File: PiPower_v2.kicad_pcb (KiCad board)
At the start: 2 copper layers, 56 x 60 mm, 80 parts, among them J1 MicroUSB_in, J10 5V_Pi, J11 12V_Out, J12 5V_IN, J2 LiPo_JST, J3 USB_A_out, J4 Auto_On, J5 5V_USB, J6 5V_EXT, J7 5V_OUT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

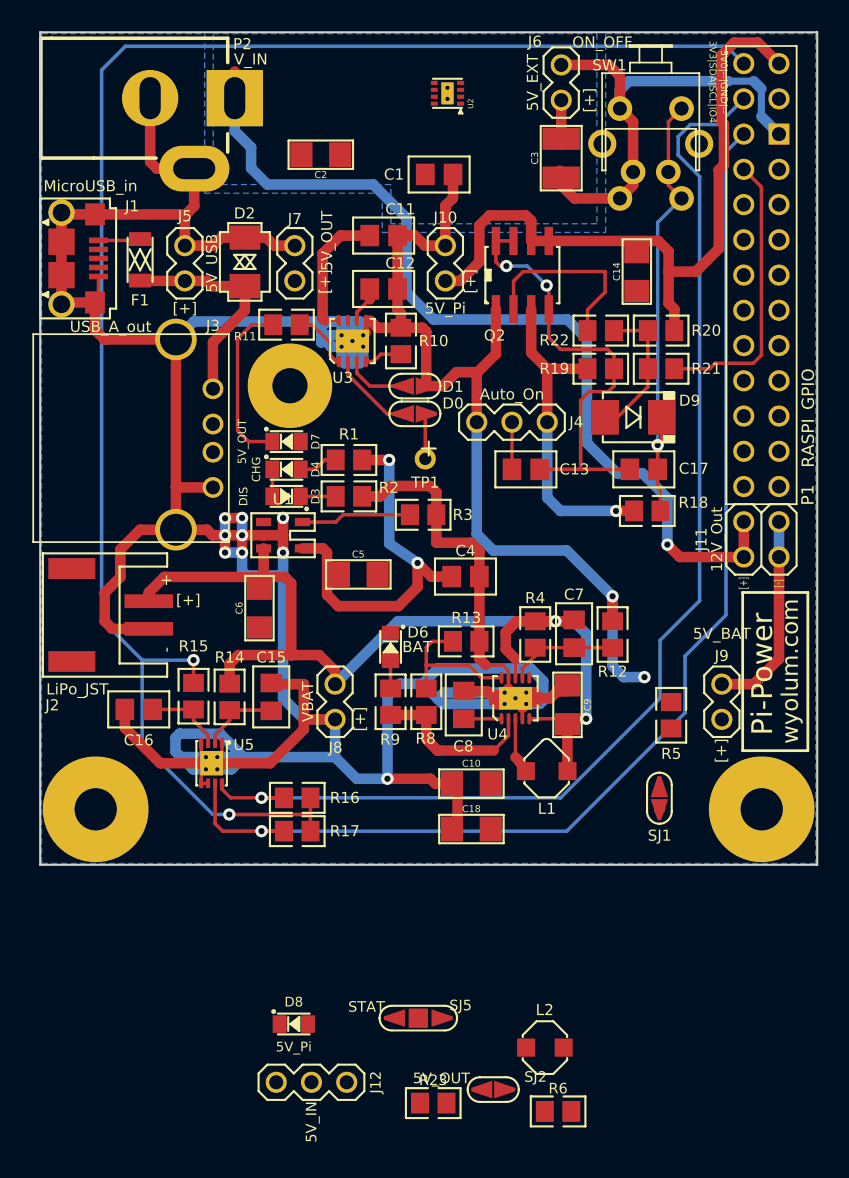
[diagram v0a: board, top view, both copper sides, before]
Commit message: 1311050158 preliminary track layout complete
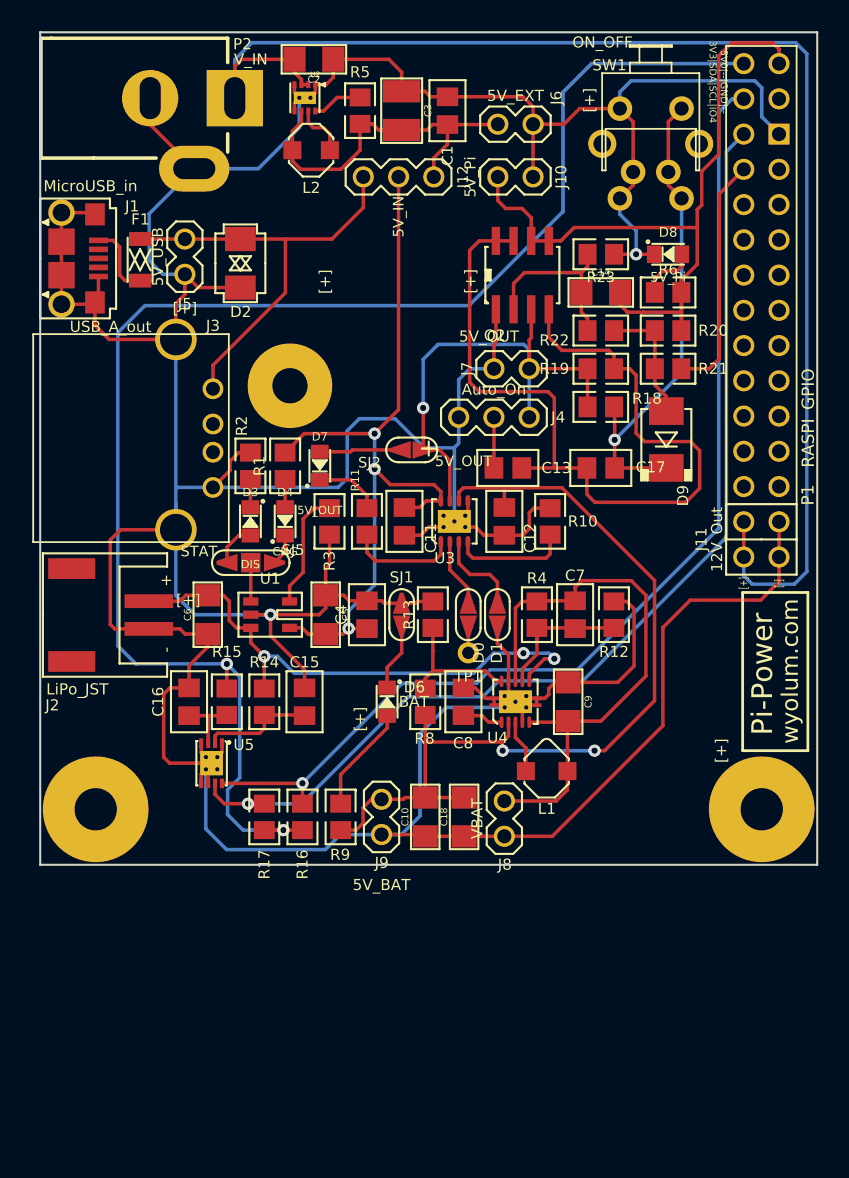
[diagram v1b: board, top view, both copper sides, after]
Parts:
- moved L2 66.8 mm to (111.3, 27.2), turned to 180 degrees
- moved J12 65.6 mm to (117.6, 29.2)
- moved R23 62.4 mm to (132.2, 34.8), turned to 180 degrees
- moved D8 61.7 mm to (137.0, 34.8)
- moved R6 59.6 mm to (137.0, 37.5)
- moved R5 49.0 mm to (114.8, 24.4), turned to 90 degrees
- moved SJ2 46.5 mm to (118.5, 48.9), turned to 180 degrees
- moved SJ5 35.0 mm to (106.9, 57.0)
- moved J9 25.9 mm to (116.3, 75.3), turned to 270 degrees
- moved SJ1 22.8 mm to (117.8, 60.7), turned to 90 degrees
- moved C11 20.7 mm to (118.0, 54.0), turned to 270 degrees
- moved C12 18.9 mm to (125.2, 54.0), turned to 270 degrees
- moved SJ4 17.5 mm to (124.7, 60.7), turned to 270 degrees
- moved J7 17.4 mm to (125.7, 43.0), turned to 180 degrees
- moved R10 16.9 mm to (128.5, 54.0)
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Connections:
- SJ5 pad 2: N-0000014 -> /STAT
- SJ5 pad 3: /STAT -> N-0000014
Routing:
- net /5V_BAT: track 14.9 -> 64.5 mm, vias 0 -> 2
- net /PWR_IN: track 66.6 -> 100.6 mm, vias 1 -> 0
- net N-0000021: track 32.7 -> 62.0 mm, vias 2 -> 0
- net /5V_EXT: track 3.18 -> 25.9 mm
- net GND: track 410.0 -> 389.3 mm, vias 11 -> 2
- net /5V_IN: track 37.3 -> 55.9 mm, vias 2 -> 3
- net /5V_USB: track 16.1 -> 32.2 mm
- net /5V_OUT: track 23.6 -> 36.1 mm
- net /SDA_Pi: track 86.6 -> 77.1 mm
- net /3V3_Pi: track 119.3 -> 109.8 mm
- net /SCL_Pi: track 87.2 -> 77.8 mm
- net N-0000035: track 12.4 -> 4.77 mm
- net /VBAT: track 74.1 -> 81.6 mm, vias 2 -> 3
- net N-0000011: track 0.00 -> 5.86 mm
- net N-000007: track 1.98 -> 7.72 mm
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- removed copper zone on B.Cu, net /5V_EXT
- removed copper zone on B.Cu, net GND

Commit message: 1311051633 track layout complete
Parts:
- moved J12 1.30 mm to (117.6, 30.5)
- moved SW1 1.00 mm to (134.8, 24.2)
- moved TP1 0.20 mm to (122.6, 63.3)
- moved J8 0.12 mm to (125.2, 75.3)
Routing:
- net GND: track 389.3 -> 404.4 mm
- net /5V_BAT: track 64.5 -> 70.4 mm
- net /3V3_Pi: track 109.8 -> 113.6 mm
- net /VBAT: track 81.6 -> 84.3 mm
- net /GPIO4: track 17.4 -> 20.1 mm
- net /5V_EXT: track 25.9 -> 28.1 mm
- net /SCL_Pi: track 77.8 -> 79.9 mm
- net /5V_Pi: track 51.0 -> 52.5 mm
- net /5V_USB: track 32.2 -> 30.9 mm
- net /5V_IN: track 55.9 -> 54.6 mm
- net /SDA_Pi: track 77.1 -> 77.8 mm
- net N-0000021: track 62.0 -> 61.5 mm
- added copper zone on B.Cu, net GND
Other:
- net class 15mil added: clearance 0.0635, trace_width 0.381, via_dia 0.889, via_drill 0.635
- board text added: "ON<>OFF"
- board text added: "rev 2"

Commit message: 1311051958 added some zones
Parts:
- moved J12 8.15 mm to (117.6, 38.6)
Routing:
- net /3V3_Pi: track 113.6 -> 101.9 mm
- net /5V_EXT: track 28.1 -> 36.3 mm
- net /5V_IN: track 54.6 -> 46.5 mm
- net /5V_USB: track 30.9 -> 28.2 mm
- net N-0000021: track 61.5 -> 60.8 mm
- net N-0000022: track 12.9 -> 12.4 mm
- added copper zone on F.Cu, net /5V_EXT
- added copper zone on F.Cu, net /5V_Pi

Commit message: 1311051125 added more zones
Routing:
- net GND: track 404.4 -> 391.6 mm
- net N-000007: track 7.72 -> 9.18 mm
- added copper zone on F.Cu, net /5V_BAT
- added copper zone on F.Cu, net /5V_USB
- added copper zone on F.Cu, net /VBAT
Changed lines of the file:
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@@
     (thickness 1.6)
     (drawings 31)
-    (tracks 606)
+    (tracks 596)
     (zones 0)
     (modules 80)
@@
   (segment (start 102.247 59.328) (end 103.825 59.328) (width 0.762) (layer F.Cu) (net 21) (status 20))
   (segment (start 101.82322 59.75178) (end 102.247 59.328) (width 0.762) (layer F.Cu) (net 21))
+  (segment (start 144.995 56.57) (end 144.995 66.955) (width 0.762) (layer F.Cu) (net 22) (status 400000))
+  (segment (start 135.38 76.57) (end 125.2 76.57) (width 0.762) (layer F.Cu) (net 22) (status 800000))
+  (segment (start 144.995 66.955) (end 135.38 76.57) (width 0.762) (layer F.Cu) (net 22))
   (segment (start 132.5275 24.25) (end 134.525 24.25) (width 0.762) (layer B.Cu) (net 22) (status 10))
   (segment (start 134.525 24.25) (end 136.525 22.25) (width 0.762) (layer B.Cu) (net 22))
@@
   (via (at 134.7 34.75) (size 0.889) (layers F.Cu B.Cu) (net 22))
   (segment (start 134.7 32.8995) (end 132.5275 30.727) (width 0.762) (layer B.Cu) (net 22) (status 20))
-  (segment (start 125.2 76.57) (end 131.43 76.57) (width 0.762) (layer F.Cu) (net 22) (status 10))
-  (segment (start 143.675 59.675) (end 144.995 58.355) (width 0.762) (layer F.Cu) (net 22))
-  (segment (start 141.8 59.675) (end 143.675 59.675) (width 0.762) (layer F.Cu) (net 22))
-  (segment (start 139.175 62.3) (end 141.8 59.675) (width 0.762) (layer F.Cu) (net 22))
-  (segment (start 139.175 68.825) (end 139.175 62.3) (width 0.762) (layer F.Cu) (net 22))
-  (segment (start 144.995 58.355) (end 144.995 56.57) (width 0.762) (layer F.Cu) (net 22) (status 20))
-  (segment (start 131.43 76.57) (end 139.175 68.825) (width 0.762) (layer F.Cu) (net 22))
   (segment (start 125.2 76.57) (end 122.427 76.57) (width 0.762) (layer F.Cu) (net 22) (status 30))
   (segment (start 122.427 76.57) (end 122.3 76.697) (width 0.762) (layer F.Cu) (net 22) (status 30))
@@
   (segment (start 101.533 40.888) (end 101.533 51.575) (width 0.762) (layer B.Cu) (net 22) (status 10))
   (segment (start 101.533 51.575) (end 101.533 54.604) (width 0.762) (layer B.Cu) (net 22) (status 20))
-  (segment (start 99.57416 61.74822) (end 97.12322 61.74822) (width 0.762) (layer F.Cu) (net 22) (status 10))
-  (segment (start 97.12322 61.74822) (end 96.8 61.425) (width 0.762) (layer F.Cu) (net 22))
-  (segment (start 96.8 61.425) (end 96.8 55.35) (width 0.762) (layer F.Cu) (net 22))
-  (segment (start 96.8 55.35) (end 97.546 54.604) (width 0.762) (layer F.Cu) (net 22))
-  (segment (start 97.546 54.604) (end 101.533 54.604) (width 0.762) (layer F.Cu) (net 22) (status 20))
   (segment (start 125.5 65.525) (end 125.5 66.31) (width 0.254) (layer F.Cu) (net 22) (status 30))
   (segment (start 125.5 66.31) (end 125.22 66.59) (width 0.254) (layer F.Cu) (net 22) (status 30))
@@
   (segment (start 128.8 50.15) (end 131.15 50.15) (width 0.254) (layer F.Cu) (net 33) (status 20))
   (segment (start 125.865 33.785) (end 124.595 33.785) (width 0.254) (layer F.Cu) (net 33) (status 30))
-  (segment (start 130.753 37.5) (end 129.575 37.5) (width 0.254) (layer F.Cu) (net 34) (status 400000))
+  (segment (start 130.753 37.5) (end 129.575 37.5) (width 0.254) (layer F.Cu) (net 34))
   (segment (start 126.425 37) (end 125.865 37.56) (width 0.254) (layer F.Cu) (net 34))
   (segment (start 129.075 37) (end 126.425 37) (width 0.254) (layer F.Cu) (net 34))
@@
   (segment (start 97.475 36.25) (end 97.875 36.65) (width 0.381) (layer F.Cu) (net 55))
   (segment (start 97.875 36.65) (end 98.95 36.65) (width 0.381) (layer F.Cu) (net 55) (status 20))
-  (segment (start 116.75 68.016) (end 116.75 68.9) (width 0.254) (layer F.Cu) (net 66) (status 10))
-  (segment (start 113.4 72.25) (end 113.4 74.3475) (width 0.254) (layer F.Cu) (net 66) (status 20))
-  (segment (start 116.75 68.9) (end 113.4 72.25) (width 0.254) (layer F.Cu) (net 66))
+  (segment (start 113.4 74.3475) (end 113.4 68.875) (width 0.254) (layer F.Cu) (net 66) (status 400000))
+  (segment (start 114.259 68.016) (end 116.75 68.016) (width 0.254) (layer F.Cu) (net 66) (status 800000))
+  (segment (start 113.4 68.875) (end 114.259 68.016) (width 0.254) (layer F.Cu) (net 66))
   (segment (start 111.575 24.425) (end 112.175 24.425) (width 0.381) (layer F.Cu) (net 69) (status 10))
   (segment (start 113.1525 23.4475) (end 114.8 23.4475) (width 0.381) (layer F.Cu) (net 69) (status 20))
   (segment (start 112.175 24.425) (end 113.1525 23.4475) (width 0.381) (layer F.Cu) (net 69))
-  (segment (start 116.75 65.984) (end 116.75 64.525) (width 0.254) (layer F.Cu) (net 70) (status 10))
-  (segment (start 117.8 63.475) (end 117.8 61.5505) (width 0.254) (layer F.Cu) (net 70) (status 20))
-  (segment (start 116.75 64.525) (end 117.8 63.475) (width 0.254) (layer F.Cu) (net 70))
+  (segment (start 116.75 65.984) (end 116.75 62.6005) (width 0.254) (layer F.Cu) (net 70) (status 400000))
+  (segment (start 116.75 62.6005) (end 117.8 61.5505) (width 0.254) (layer F.Cu) (net 70) (status 800000))
   (zone (net 22) (net_name GND) (layer B.Cu) (hatch edge 0.508)
     (connect_pads (clearance 0.508))
@@
       )
     )
+  )
+  (zone (net 21) (net_name /VBAT) (layer F.Cu) (hatch edge 0.508)
+    (connect_pads (clearance 0.508))
+    (min_thickness 0.254)
+    (fill (arc_segments 16) (thermal_gap 0.508) (thermal_bridge_width 0.508))
+    (polygon
+      (pts
+        (xy 113.325 78.675) (xy 91.825 78.675) (xy 91.825 56.525) (xy 113.325 56.525)
+      )
+    )
+  )
+  (zone (net 7) (net_name /5V_USB) (layer F.Cu) (hatch edge 0.508)
+    (connect_pads (clearance 0.508))
+    (min_thickness 0.254)
+    (fill (arc_segments 16) (thermal_gap 0.508) (thermal_bridge_width 0.508))
+    (polygon
+      (pts
+        (xy 115.825 55.775) (xy 91.825 55.775) (xy 91.825 30.775) (xy 107.175 30.775) (xy 107.175 37.925)
+        (xy 115.825 37.925)
+      )
+    )
+  )
+  (zone (net 2) (net_name /5V_BAT) (layer F.Cu) (hatch edge 0.508)
+    (connect_pads (clearance 0.508))
+    (min_thickness 0.254)
+    (fill (arc_segments 16) (thermal_gap 0.508) (thermal_bridge_width 0.508))
+    (polygon
+      (pts
+        (xy 147.675 78.675) (xy 114.075 78.675) (xy 114.075 56.525) (xy 147.675 56.525)
+      )
+    )

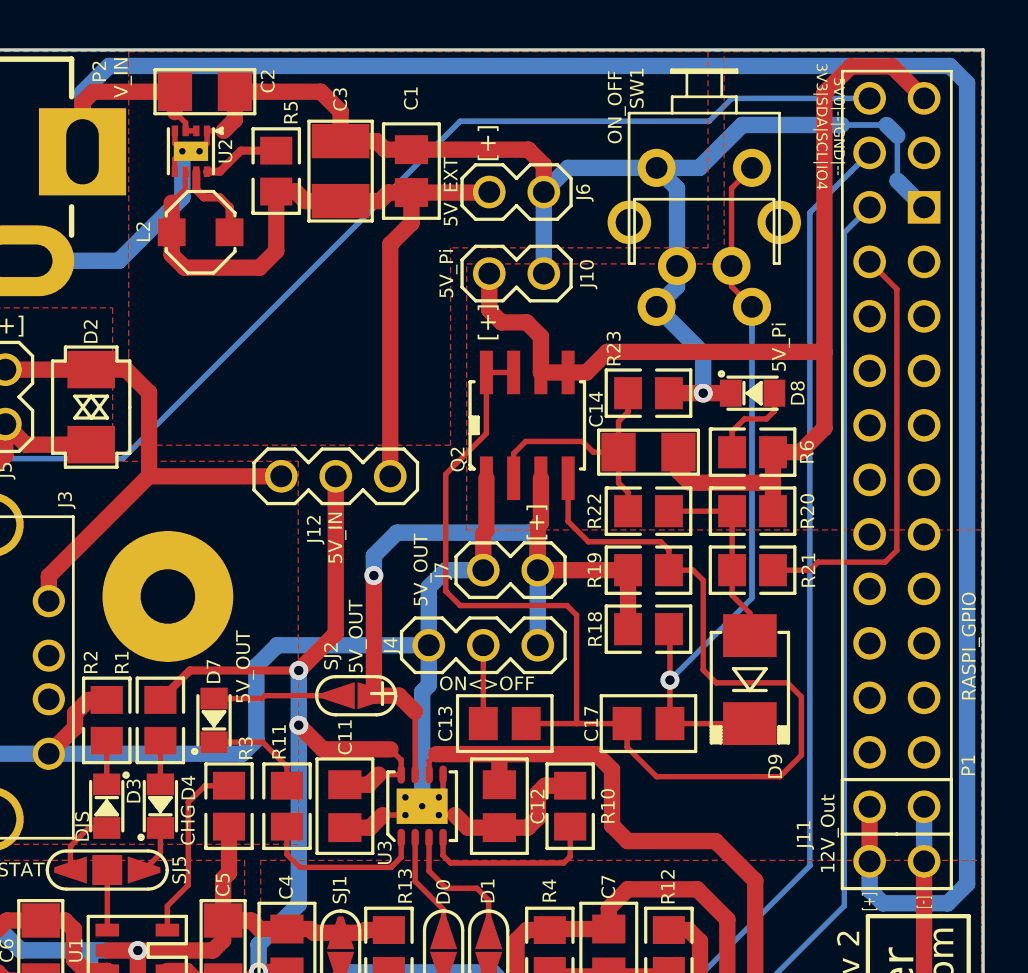
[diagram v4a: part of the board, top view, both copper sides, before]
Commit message: 1311060933 changed some resistor values for charging current and LEDs
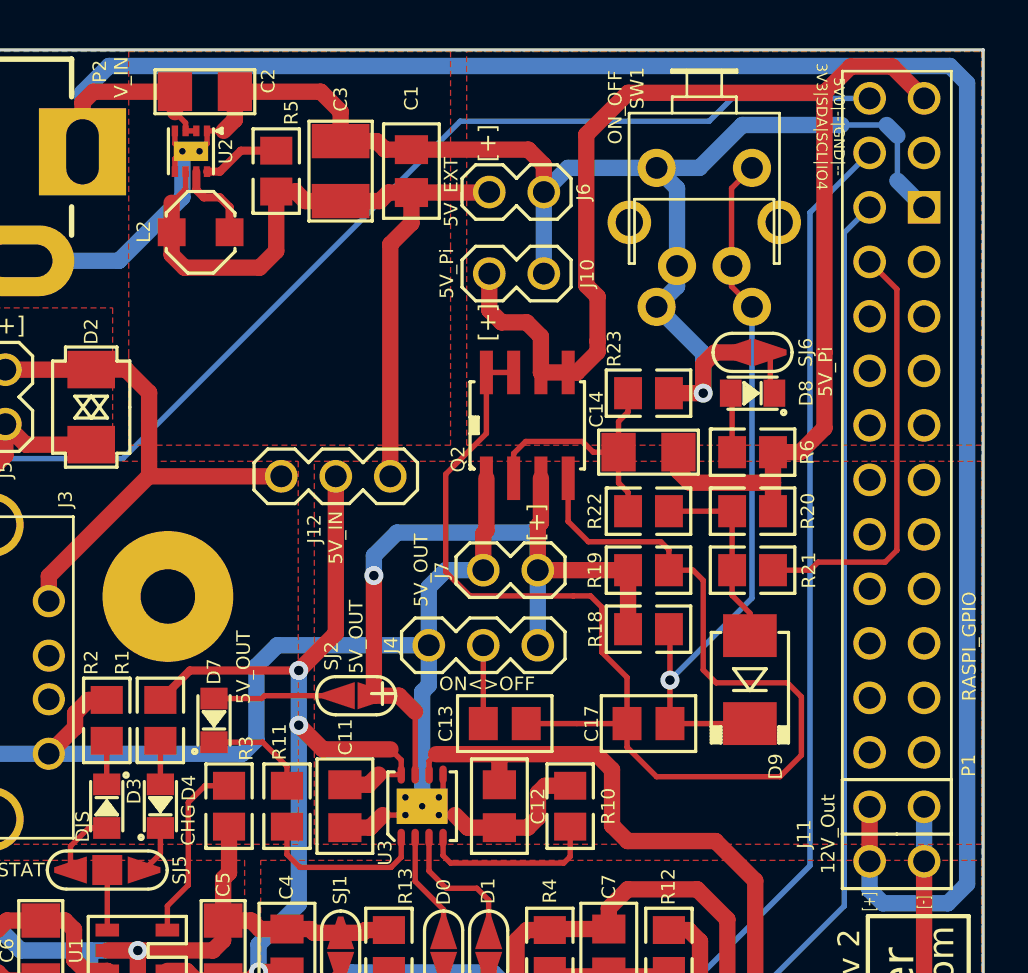
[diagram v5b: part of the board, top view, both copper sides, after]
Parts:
- added SJ6: 5V_Pi, ShortLink, F.Cu at (137.0, 32.9)
- R1, R2, R6, R9: value 4k7 -> 2k2
- R3: value 4k7 -> 2k
- turned D8 to 180 degrees
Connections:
- D8 pad 2: GND -> N-0000015
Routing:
- net /5V_Pi: track 52.5 -> 64.1 mm
- net N-0000015: track 0.00 -> 1.98 mm
- net GND: track 391.6 -> 393.4 mm
- net N-0000024: track 4.17 -> 2.78 mm
- net N-0000021: track 60.8 -> 62.1 mm
- added copper zone on F.Cu, net /5V_IN

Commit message: 1311081530 changed board size to 56x56mm, Gerbers ready
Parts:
- moved J8 11.4 mm to (132.9, 67.0), turned to 90 degrees
- moved R9 8.29 mm to (114.2, 67.0)
- moved H1 4.00 mm to (95.8, 70.8)
- moved H2 4.00 mm to (143.8, 70.8)
- moved C10 3.40 mm to (119.5, 71.9)
- moved C18 3.40 mm to (122.3, 71.9)
- moved J9 3.40 mm to (116.3, 71.9)
- moved R16 3.00 mm to (110.7, 72.3)
- moved R17 3.00 mm to (107.9, 72.3)
- moved PCB1 2.00 mm to (119.8, 46.8)
- moved L1 1.50 mm to (129.8, 72.0)
- moved U5 0.52 mm to (104.1, 72.0)
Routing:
- net /3V3_Pi: track 101.9 -> 96.2 mm
- net N-000006: track 9.18 -> 3.82 mm
- net /VBAT: track 84.3 -> 79.5 mm
- net /SDA_Pi: track 77.8 -> 80.7 mm
- net /5V_BAT: track 70.4 -> 67.8 mm, vias 2 -> 0
- net /L: track 3.84 -> 5.19 mm
- net /SCL_Pi: track 79.9 -> 81.2 mm
- net GND: track 393.4 -> 392.5 mm, vias 2 -> 3
- net N-000002: track 8.19 -> 8.71 mm
- net N-000005: track 4.77 -> 5.29 mm
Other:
- board size 56 x 60 mm -> 56 x 56 mm
- board text added: "USB<>BARREL"
